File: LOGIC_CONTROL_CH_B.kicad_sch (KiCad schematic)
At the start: 47 parts, among them IC1701 ${DEVICE}, IC1702 ${DEVICE}, IC1703 ${DEVICE}, IC1704 ${DEVICE}, IC1705 ${DEVICE}, IC1706 ${DEVICE}, IC1707 ${DEVICE}

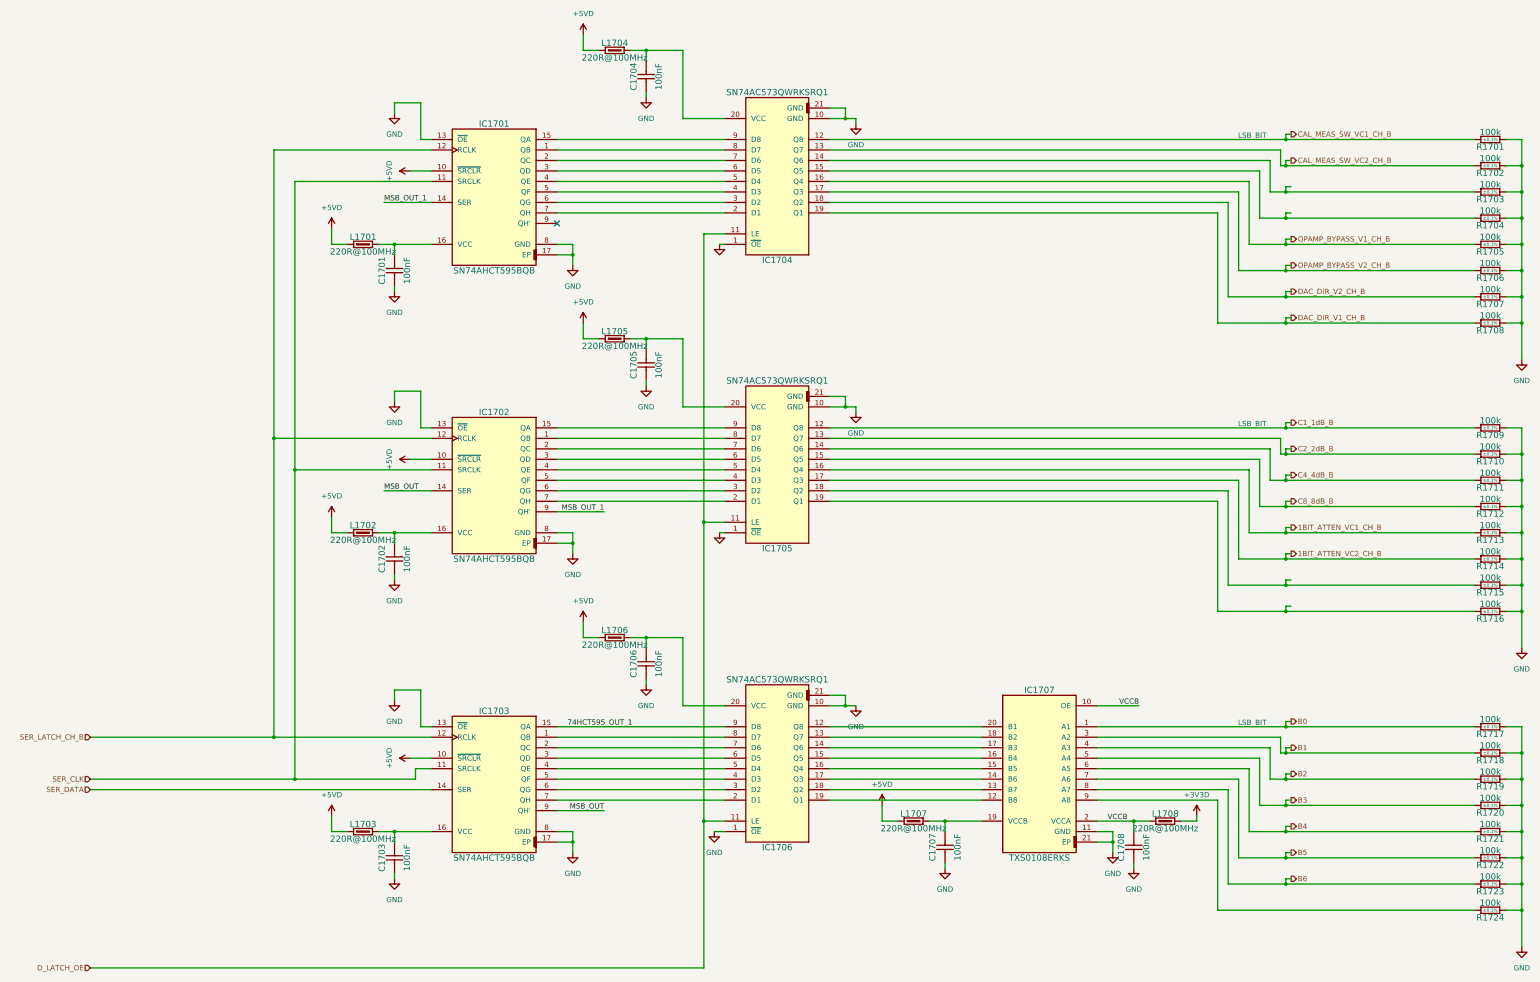
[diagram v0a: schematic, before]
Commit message: New channels topolgy added
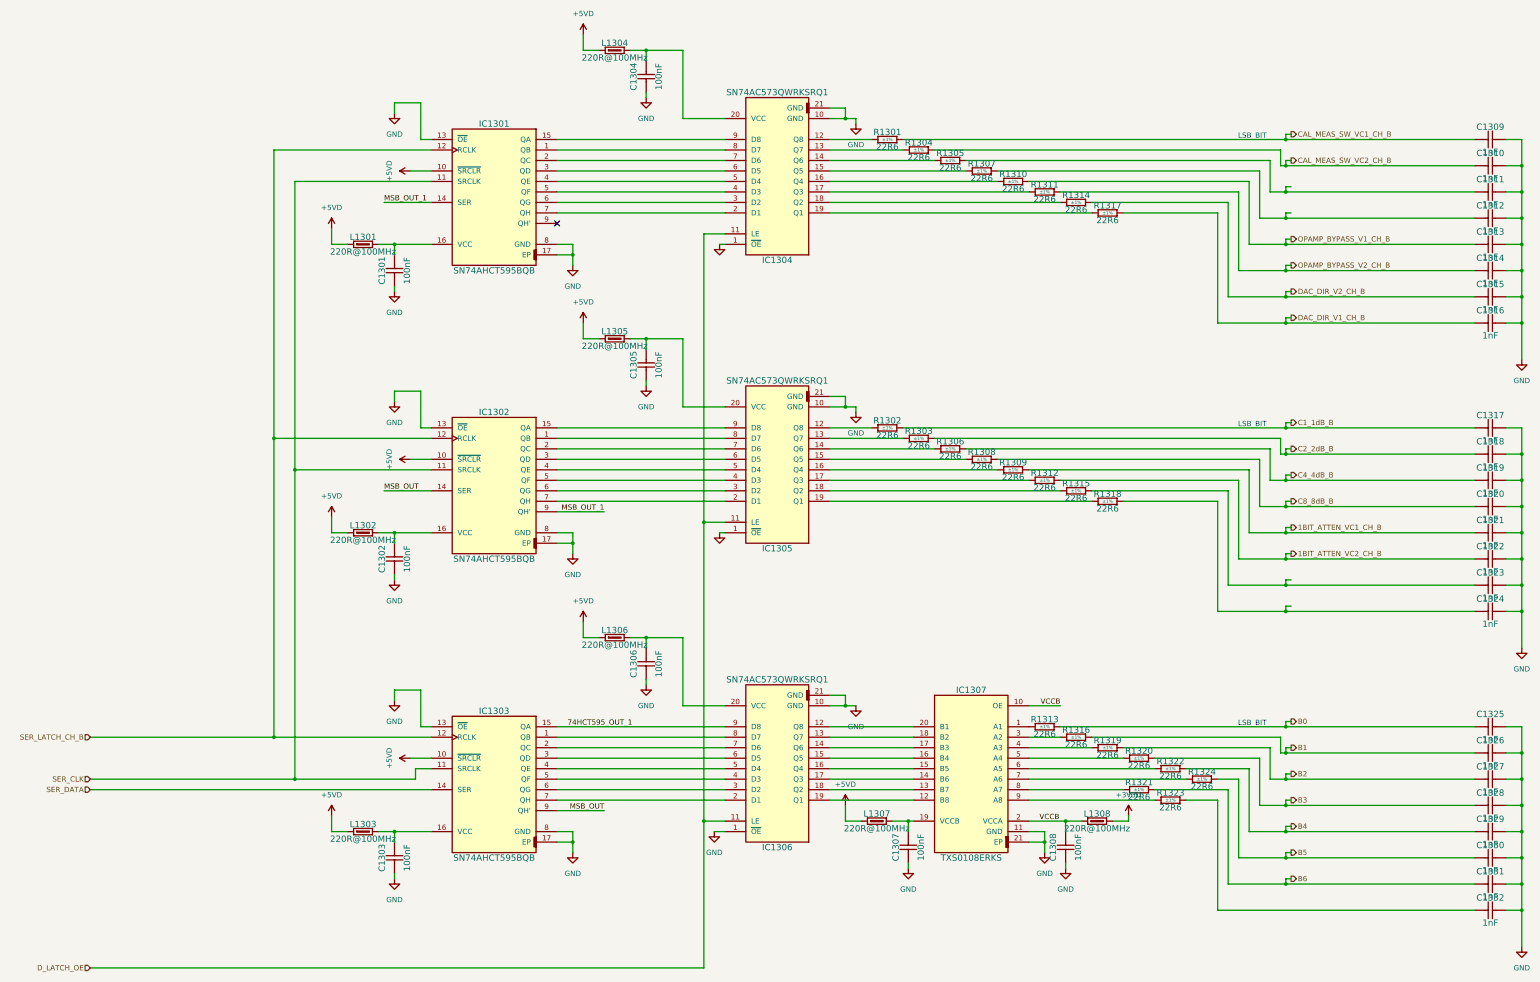
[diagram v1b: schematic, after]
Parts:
- removed R1701, R1702, R1703, R1704, R1705, R1706, R1707, R1708, R1709, R1710, R1711, R1712, R1713, R1714, R1715, R1716, R1717, R1718, R1719, R1720, R1721, R1722, R1723, R1724: 100k, Resistors SMD:RESC1005X35N, symbol CERN:Resistors SMD/R0402_10K_0.1%_0.063W_25PPM
- added C1309, C1310, C1311, C1312, C1313, C1314, C1315, C1316, C1317, C1318, C1319, C1320, C1321, C1322, C1323, C1324, C1325, C1326, C1327, C1328, C1329, C1330, C1331, C1332: 1nF, Capacitors SMD:CAPC1005X55N, symbol CERN:Capacitors SMD/CC0402_1NF_50V_5%_C0G
- added R1301, R1302, R1303, R1304, R1305, R1306, R1307, R1308, R1309, R1310, R1311, R1312, R1313, R1314, R1315, R1316, R1317, R1318, R1319, R1320, R1321, R1322, R1323, R1324: 22R6, Resistors SMD:RESC1005X40N, symbol CERN:Resistors SMD/R0402_22R6_1%_0.063W_100PPM
- renumbered C1701 to C1301, C1702 to C1302, C1703 to C1303, C1704 to C1304, C1705 to C1305, C1706 to C1306, C1707 to C1307, C1708 to C1308, IC1701 to IC1301, IC1702 to IC1302, IC1703 to IC1303, IC1704 to IC1304, IC1705 to IC1305, IC1706 to IC1306, IC1707 to IC1307, L1701 to L1301, L1702 to L1302, L1703 to L1303, L1704 to L1304, L1705 to L1305, L1706 to L1306, L1707 to L1307, L1708 to L1308
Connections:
- net 1BIT_ATTEN_VC1_CH_B: now also C1321.1, R1309.2; no longer IC1305.16 (Q4)
- net 1BIT_ATTEN_VC2_CH_B: now also C1322.1, R1312.2; no longer IC1305.17 (Q3)
- net B0: now also C1325.1, R1313.2; no longer IC1307.1 (A1)
- net B1: now also C1326.1, R1316.2; no longer IC1307.3 (A2)
- net B2: now also C1327.1, R1319.2; no longer IC1307.4 (A3)
- net B3: now also C1328.1, R1320.2; no longer IC1307.5 (A4)
- net B4: now also C1329.1, R1322.2; no longer IC1307.6 (A5)
- net B5: now also C1330.1, R1324.2; no longer IC1307.7 (A6)
- net B6: now also C1331.1, R1321.2; no longer IC1307.8 (A7)
- net C1_1dB_B: now also C1317.1, R1302.2; no longer IC1305.12 (Q8)
- net C2_2dB_B: now also C1318.1, R1303.2; no longer IC1305.13 (Q7)
- net C4_4dB_B: now also C1319.1, R1306.2; no longer IC1305.14 (Q6)
- net C8_8dB_B: now also C1320.1, R1308.2; no longer IC1305.15 (Q5)
- net CAL_MEAS_SW_VC1_CH_B: now also C1309.1, R1301.2; no longer IC1304.12 (Q8)
- net CAL_MEAS_SW_VC2_CH_B: now also C1310.1, R1304.2; no longer IC1304.13 (Q7)
- net DAC_DIR_V1_CH_B: now also C1316.1, R1317.2; no longer IC1304.19 (Q1)
- net DAC_DIR_V2_CH_B: now also C1315.1, R1314.2; no longer IC1304.18 (Q2)
- net GND: now also C1309.2, C1310.2, C1311.2, C1312.2, C1313.2, C1314.2, C1315.2, C1316.2, C1317.2, C1318.2, C1319.2, C1320.2, C1321.2, C1322.2, C1323.2, C1324.2, C1325.2, C1326.2, C1327.2, C1328.2, C1329.2, C1330.2, C1331.2, C1332.2
- net OPAMP_BYPASS_V1_CH_B: now also C1313.1, R1310.2; no longer IC1304.16 (Q4)
- net OPAMP_BYPASS_V2_CH_B: now also C1314.1, R1311.2; no longer IC1304.17 (Q3)
- net at IC1305.18 (Q2): now also R1315.1
- net at IC1307.9 (A8): now also R1323.1
- net at IC1305.19 (Q1): now also R1318.1
- net at IC1304.15 (Q5): now also R1307.1
- net at IC1304.14 (Q6): now also R1305.1
- new net: IC1305.14 (Q6), R1306.1
- new net: C1323.1, R1315.2
- new net: IC1305.16 (Q4), R1309.1
- new net: C1332.1, R1323.2
- new net: C1324.1, R1318.2
- new net: IC1304.17 (Q3), R1311.1
- new net: IC1307.7 (A6), R1324.1
- new net: IC1307.5 (A4), R1320.1
- new net: IC1307.3 (A2), R1316.1
- new net: C1311.1, R1305.2
- new net: IC1307.6 (A5), R1322.1
- new net: C1312.1, R1307.2
- new net: IC1304.18 (Q2), R1314.1
- new net: IC1305.12 (Q8), R1302.1
- new net: IC1305.13 (Q7), R1303.1
- new net: IC1305.15 (Q5), R1308.1
- new net: IC1305.17 (Q3), R1312.1
- new net: IC1304.13 (Q7), R1304.1
- new net: IC1304.16 (Q4), R1310.1
- new net: IC1304.12 (Q8), R1301.1
- new net: IC1307.4 (A3), R1319.1
- new net: IC1304.19 (Q1), R1317.1
- new net: IC1307.1 (A1), R1313.1
- new net: IC1307.8 (A7), R1321.1
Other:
- moved on the sheet: C1307, C1308, IC1307, L1307, L1308

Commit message: Routing new channels
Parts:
- renumbered C1301 to C1701, C1302 to C1702, C1303 to C1703, C1304 to C1704, C1305 to C1705, C1306 to C1706, C1307 to C1707, C1308 to C1708, C1309 to C1709, C1310 to C1710, C1311 to C1711, C1312 to C1712, C1313 to C1713, C1314 to C1714, C1315 to C1715, C1316 to C1716, C1317 to C1717, C1318 to C1718, C1319 to C1719, C1320 to C1720, C1321 to C1721, C1322 to C1722, C1323 to C1723, C1324 to C1724, C1325 to C1725, C1326 to C1726, C1327 to C1727, C1328 to C1728, C1329 to C1729, C1330 to C1730, C1331 to C1731, C1332 to C1732, IC1301 to IC1701, IC1302 to IC1702, IC1303 to IC1703, IC1304 to IC1704, IC1305 to IC1705, IC1306 to IC1706, IC1307 to IC1707, L1301 to L1701, L1302 to L1702, L1303 to L1703, L1304 to L1704, L1305 to L1705, L1306 to L1706, L1307 to L1707, L1308 to L1708, R1301 to R1701, R1302 to R1702, R1303 to R1703, R1304 to R1704, R1305 to R1705, R1306 to R1706, R1307 to R1707, R1308 to R1708, R1309 to R1709, R1310 to R1710, R1311 to R1711, R1312 to R1712, R1313 to R1713, R1314 to R1714, R1315 to R1715, R1316 to R1716, R1317 to R1717, R1318 to R1718, R1319 to R1719, R1320 to R1720, R1321 to R1721, R1322 to R1722, R1323 to R1723, R1324 to R1724
